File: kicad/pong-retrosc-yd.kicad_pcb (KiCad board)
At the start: 2 copper layers, 55 x 88 mm, 24 parts, among them J1 RCA video (na placa), J4 chave A/B (painel), J5 pot P1 (painel), J6 pot P2 (painel), J7 START (painel), J8 RCA audio L (na placa), J9 RCA audio R (na placa), U1 RP2040 roxo 1 botao, U2 PAM8403 HW-012

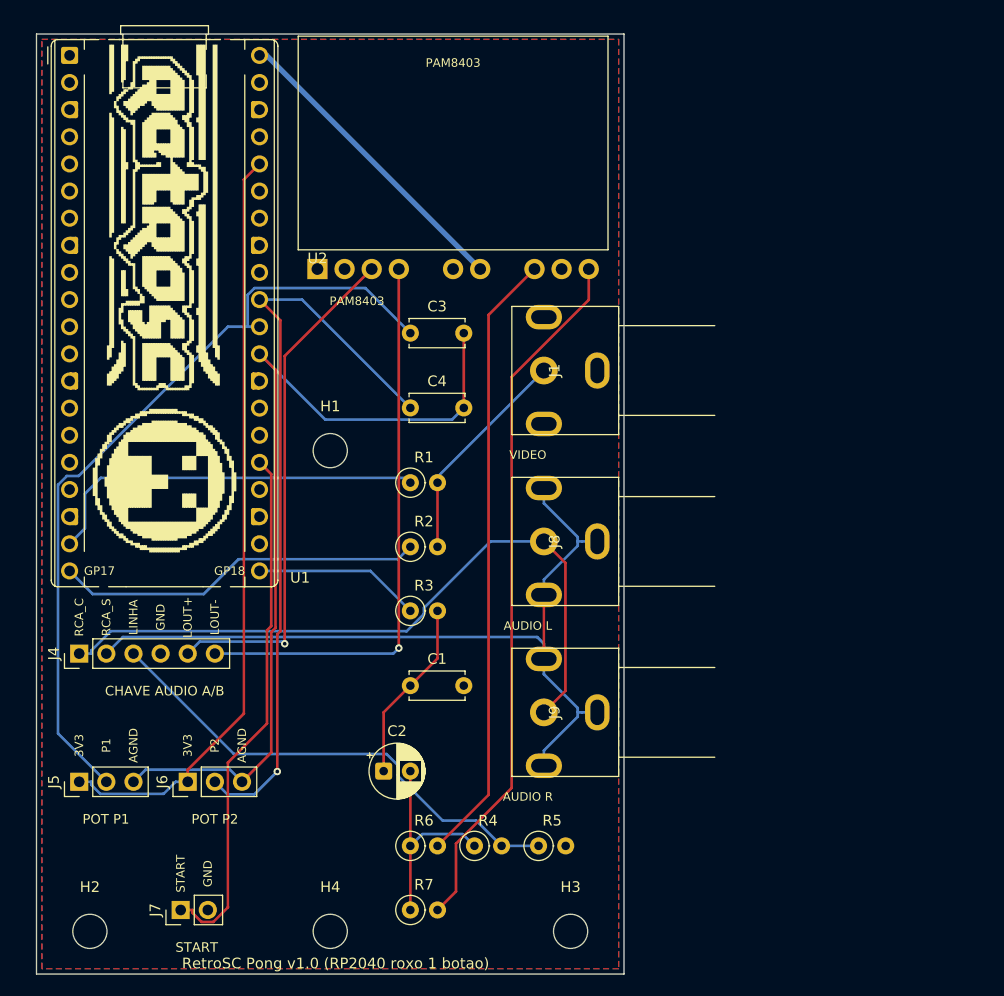
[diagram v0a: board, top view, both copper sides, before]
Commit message: kicad: placa 80x66 para a caixa Patola PB-085/3 (DRC 0 erros)
A placa era 55 x 88 e nao entrava na caixa. Agora e 80 x 66, contra os
~82 x 70 internos da PB-085/3 (85 x 73 x 32 montada).

Furacao refeita para os bossos da TAMPA: eram 4 furos M3 em losango de
45 mm; agora sao 2 furos a 58 mm entre centros, na linha de centro da
largura -- que e o que a caixa oferece (2 bossos com furo-guia o2,5, a
58 mm, no meio do lado de 85 mm). Em troca, o miolo das bordas de cima e
de baixo (x 36,5..43,5) virou area reservada.

Rearranjo, ja que a placa deitou (80 no maior lado):
- Pico a esquerda, USB na borda de cima; PAM8403 no topo a direita, com o
  pot saindo pela mesma borda
- os 3 RCAs desceram para a borda direita abaixo do amp
- os headers de painel foram para UMA fileira na borda de baixo (duas nao
  cabem: cada uma precisa de ~9 mm com os rotulos de funcao)
- rotulos dos headers centralizados sobre cada conector (PCB_TEXT e
  centrado na coordenada -- antes "CHAVE AUDIO A/B" saia cortado)

As duas variantes roteiam com 0 erros e 0 desconectados; gerbers, ZIPs e
imagens regenerados. Docs atualizados com as dimensoes, a furacao e o
aviso de que RCAs, pot e USB atravessam as paredes da caixa.

Co-Authored-By: Claude Opus 5 <noreply@anthropic.com>
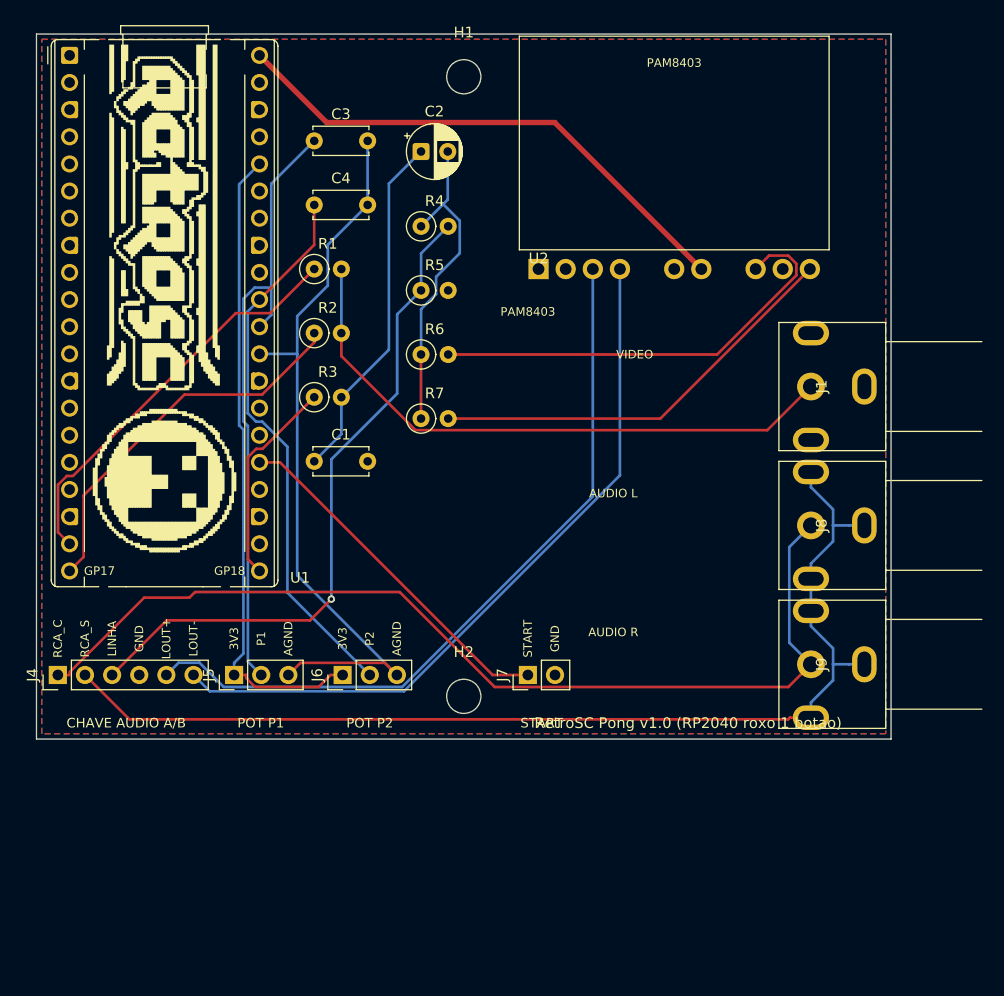
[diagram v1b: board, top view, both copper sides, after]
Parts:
- removed H3, H4: MountingHole_3.2mm_M3, MountingHole_3.2mm_M3
- moved R4 58.2 mm to (56.0, 38.0)
- moved C2 58.1 mm to (56.0, 31.0)
- moved R5 53.2 mm to (56.0, 44.0)
- moved R6 46.0 mm to (56.0, 50.0)
- moved R7 46.0 mm to (56.0, 56.0)
- moved H2 41.3 mm to (60.0, 82.0)
- moved J7 39.2 mm to (66.0, 80.0)
- moved H1 37.2 mm to (60.0, 24.0)
- moved J9 25.4 mm to (92.5, 79.0)
- moved J1 25.0 mm to (92.5, 53.0)
- moved J8 25.0 mm to (92.5, 66.0)
- moved C1 22.8 mm to (46.0, 60.0)
- moved R1 21.9 mm to (46.0, 42.0)
- moved R2 21.9 mm to (46.0, 48.0)
- moved R3 21.9 mm to (46.0, 54.0)
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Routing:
- net COMPOSITE: track 20.6 -> 56.7 mm
- net RCA_C: track 66.0 -> 93.1 mm
- net AMP_R: track 65.9 -> 39.7 mm
- net RCA_S: track 78.2 -> 102.0 mm
- net LOUT_P: track 48.1 -> 70.0 mm, vias 1 -> 0
- net +5V: track 28.9 -> 49.6 mm
- net POT2: track 70.6 -> 51.6 mm, vias 1 -> 0
- net LINHA: track 45.9 -> 62.9 mm, vias 0 -> 1
- net POT1: track 74.9 -> 58.5 mm
- net AMP_L: track 57.8 -> 41.4 mm
- net AUD_F: track 17.1 -> 33.1 mm
- net START: track 49.4 -> 33.4 mm
- net LOUT_N: track 52.9 -> 68.2 mm, vias 1 -> 0
- net +3V3: track 71.9 -> 60.4 mm
- net AGND: track 82.2 -> 71.2 mm
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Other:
- board size 55 x 88 mm -> 80 x 66 mm

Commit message: kicad: cobre longe dos parafusos e serigrafia corrigida
Dois problemas apontados na revisao da placa.

1. Trilhas rentes aos furos de montagem: o roteador passava sinal a 2,0 mm
   do centro do furo -- 0,4 mm da borda, debaixo da cabeca do parafuso.
   Agora cada furo tem uma AREA DE EXCLUSAO de raio 3,6 mm (rule area nas
   2 faces) barrando trilha e via; o plano de GND continua entrando, que
   encostar em GND e inofensivo. A trilha mais proxima passou de 2,0 para
   3,9 mm. make_decoy.py preserva as rule areas (antes removia todas as
   zonas, e o roteador nao as via).

2. Serigrafia:
   - GP17/GP18 nao diziam QUAL pino, ao lado de 20 pads iguais: agora tem
     linha de chamada ate o pad, comecando fora do contorno do modulo
   - VIDEO/AUDIO L/AUDIO R estavam soltos no meio da placa, a 17 mm dos
     jacks: foram para junto de cada um, com a referencia (ex.: "VIDEO (J1)")
   - referencias que caiam sobre pads (J1/J4..J9, H1/H2, U2) ocultadas ou
     movidas -- a informacao esta nos rotulos descritivos
   - contorno do footprint do RCA cruzava as proprias abas de terra: as
     laterais agora sao quebradas na altura dos pads
   - logo reescalado (0,22 -> 0,19 mm/px) para caber ENTRE as duas linhas
     verticais do footprint do Pico, que ele atravessava
   - texto de versao foi para a area livre do meio (o da variante YD nao
     cabia no rodape)

   silk_over_copper 11 -> 0, silk_overlap 30 -> 0. Sobram 12 avisos de
   borda: USB e barris dos RCAs cruzando o contorno, que e intencional.

Na variante YD o roteador agora recebe 0,17 mm de isolamento: pedindo os
0,15 do projeto ele entregava 0,1478 e o DRC reprovava.

DRC: 0 erros nas duas placas. Gerbers, ZIPs, renders e desenho de encaixe
regenerados.

Co-Authored-By: Claude Opus 5 <noreply@anthropic.com>
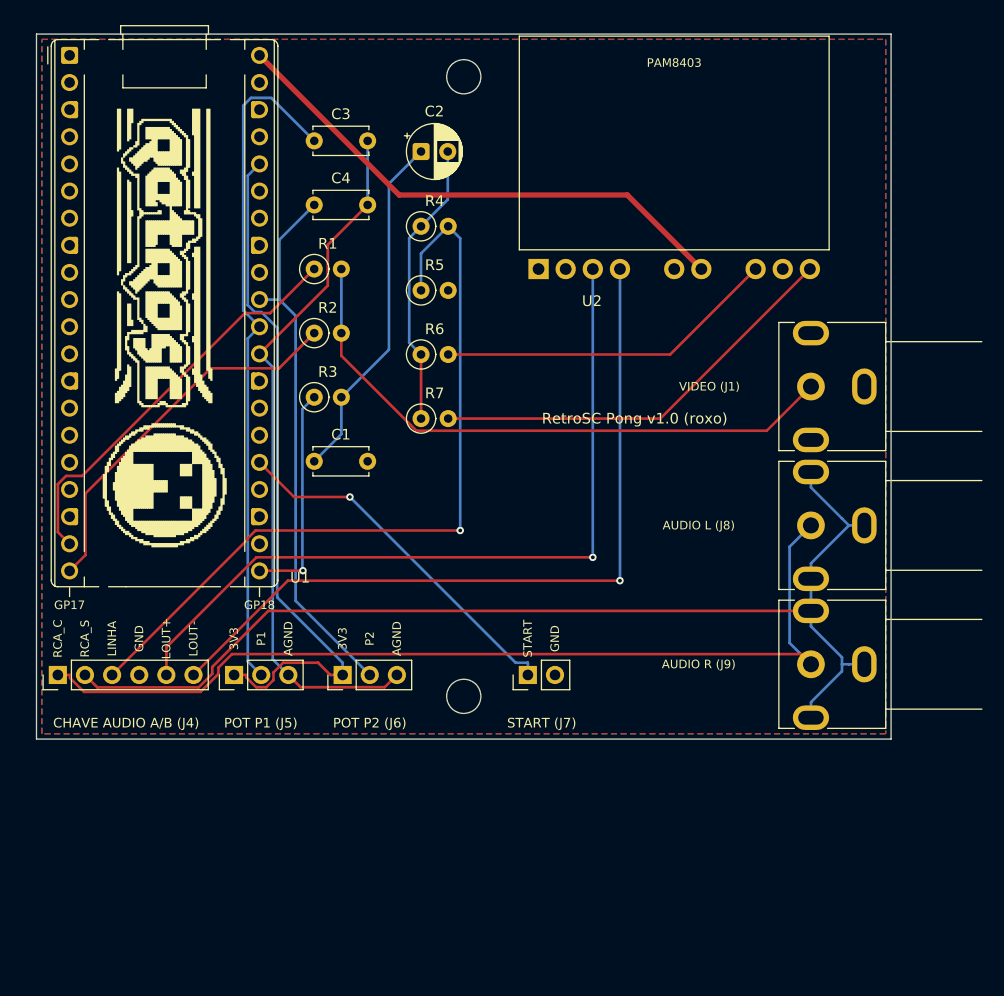
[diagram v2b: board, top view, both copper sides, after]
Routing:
- net LINHA: track 62.9 -> 74.2 mm
- net AMP_L: track 41.4 -> 32.1 mm
- net POT1: track 58.5 -> 63.5 mm
- net RCA_C: track 93.1 -> 88.2 mm
- net AGND: track 71.2 -> 66.4 mm
- net +3V3: track 60.4 -> 65.0 mm
- net LOUT_N: track 68.2 -> 72.7 mm, vias 0 -> 1
- net AUD_C: track 30.3 -> 27.0 mm
- net LOUT_P: track 70.0 -> 73.0 mm, vias 0 -> 1
- net RCA_S: track 102.0 -> 103.7 mm
- net AUDIO_PWM: track 19.6 -> 20.8 mm, vias 0 -> 1
- net POT2: track 51.6 -> 50.7 mm
- net START: track 33.4 -> 34.0 mm, vias 0 -> 1
- net VIDEO: track 36.0 -> 35.5 mm
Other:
- board text added: "AUDIO L (J8)"
- board text added: "AUDIO R (J9)"
- board text added: "CHAVE AUDIO A/B (J4)"
- board text added: "POT P1 (J5)"
- board text added: "POT P2 (J6)"
- board text added: "RetroSC Pong v1.0 (roxo)"
- board text added: "START (J7)"
- board text added: "VIDEO (J1)"
- board text removed: "AUDIO L"
- board text removed: "AUDIO R"
- board text removed: "CHAVE AUDIO A/B"
- board text removed: "PAM8403"
- board text removed: "POT P1"
- board text removed: "POT P2"
- board text removed: "RetroSC Pong v1.0 (RP2040 roxo 1 botao)"
- board text removed: "VIDEO"

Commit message: kicad: afasta os headers na borda de baixo
J4 e J5 ficavam a 0,26 mm um do outro e as descricoes ("CHAVE AUDIO A/B
(J4)" / "POT P1 (J5)") corriam juntas.

Nao dava para so espacar: J4+J5+J6 ocupavam 35,0 mm dos 36,4 disponiveis
ate a area de exclusao do furo, e o par J5/J6 e indivisivel (a vaga entre
eles existe para um unico conector femea 1x7 servir os dois). Entao quem
mudou de lugar foi o START, que e independente:

  antes:  J4  J5 J6 ......... J7
  agora:  J4 ..... J7 ..... J5 J6      (o par a direita do furo)

Folgas: 7,8 mm entre J4 e J7 e 14,9 mm entre J7 e J5. O rotulo do J9
subiu, que o par passou a ocupar a faixa onde ele estava.

DRC 0 erros nas duas placas; serigrafia sem sobreposicao nem silk sobre
cobre. Gerbers, ZIPs, renders e desenho de encaixe regenerados.

Co-Authored-By: Claude Opus 5 <noreply@anthropic.com>
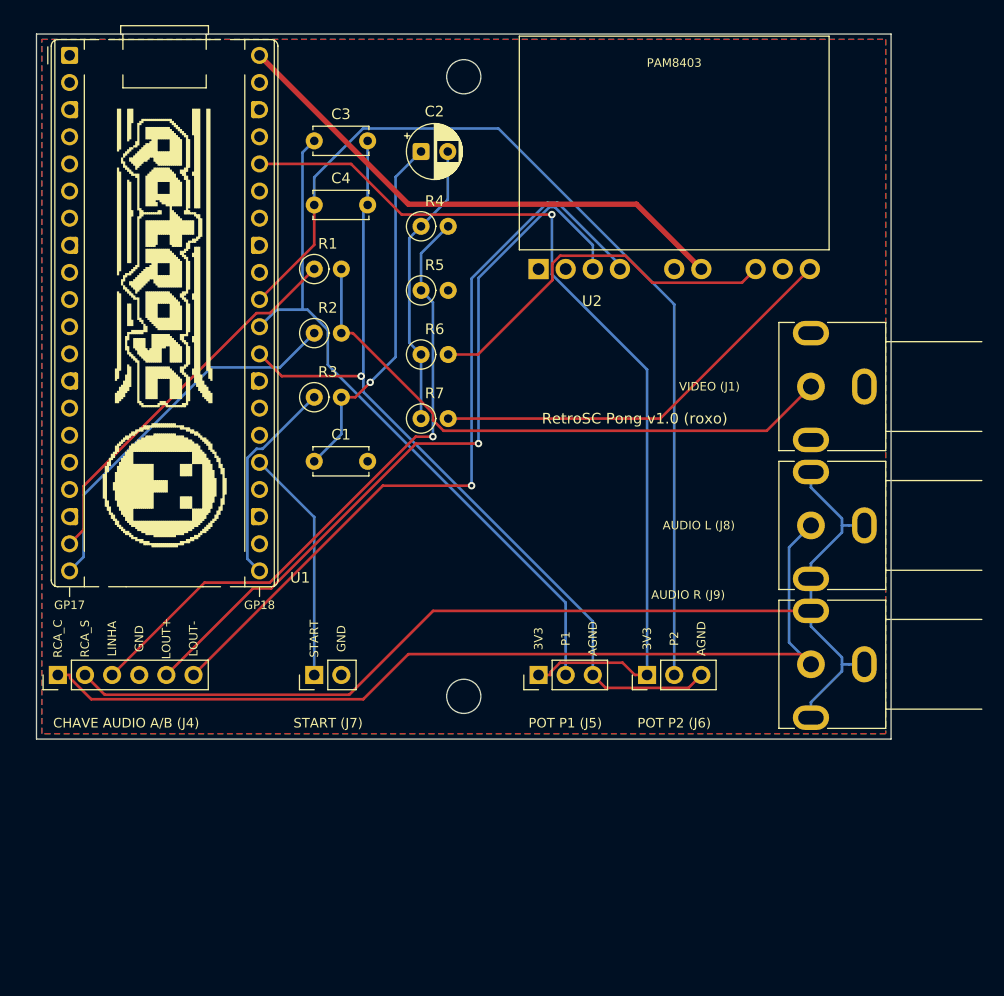
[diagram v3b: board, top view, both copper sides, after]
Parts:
- moved J5 28.5 mm to (67.0, 80.0)
- moved J6 28.5 mm to (77.2, 80.0)
- moved J7 20.0 mm to (46.0, 80.0)
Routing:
- net POT2: track 50.7 -> 90.7 mm
- net +3V3: track 65.0 -> 87.4 mm, vias 0 -> 1
- net AGND: track 66.4 -> 80.8 mm, vias 0 -> 1
- net LINHA: track 74.2 -> 60.5 mm
- net START: track 34.0 -> 22.0 mm, vias 1 -> 0
- net AMP_L: track 32.1 -> 35.1 mm
- net SYNC: track 38.4 -> 35.9 mm
- net LOUT_P: track 73.0 -> 70.9 mm
- net POT1: track 63.5 -> 65.6 mm
- net AUDIO_PWM: track 20.8 -> 19.7 mm, vias 1 -> 0
- net COMPOSITE: track 56.7 -> 55.8 mm
- net AUD_F: track 33.1 -> 33.9 mm, vias 0 -> 1

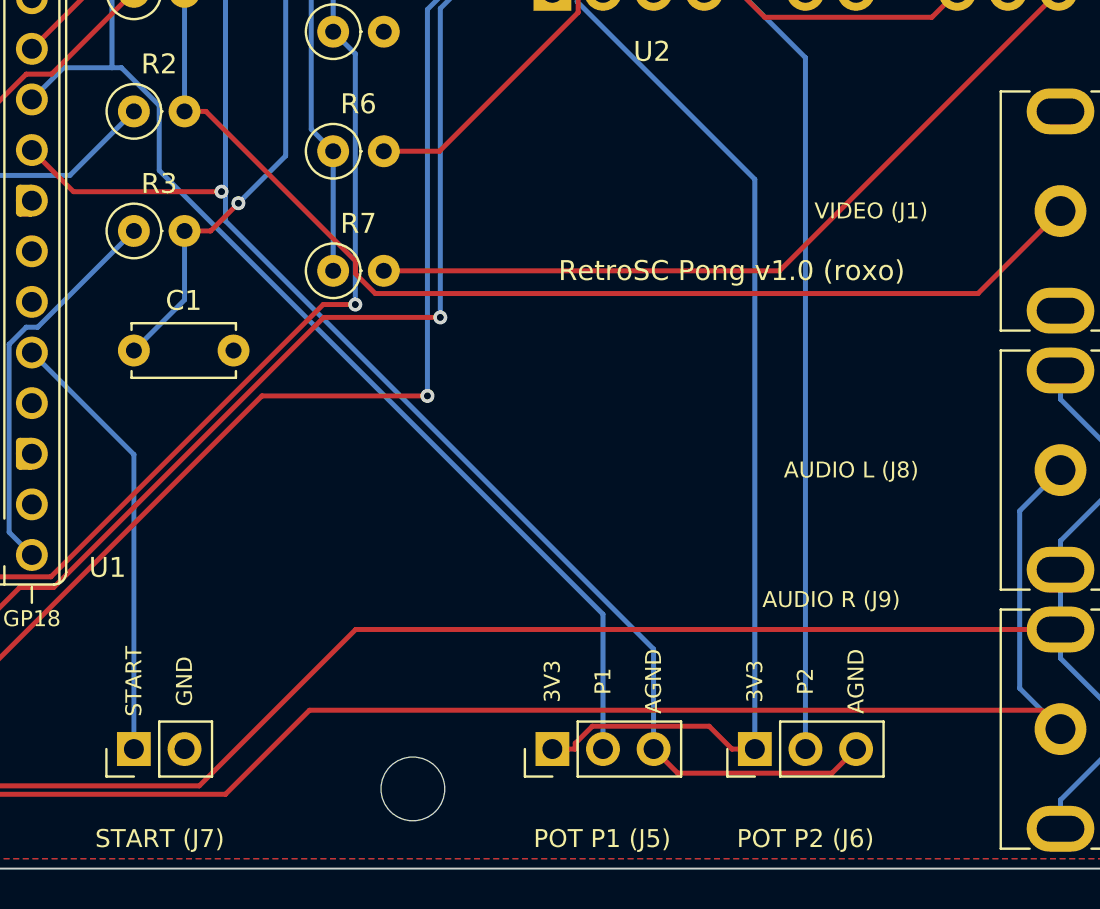
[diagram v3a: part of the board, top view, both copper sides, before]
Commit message: kicad: rotulos dos RCAs na vertical e assinatura no meio da placa
- VIDEO/AUDIO L/AUDIO R passam a ser verticais (rot 90), encostados na
  lateral de cada jack: acompanham a altura do conector, ficam sem duvida
  de qual e qual e nao disputam espaco com a faixa dos headers. O
  "AUDIO R" em especial estava solto, longe do seu jack.
- assinatura na area vazia do centro: "RetroSC Pong v1.0" em 1,6 mm e
  "LRRosa 2026" em 1,1 mm logo abaixo.

DRC 0 erros nas duas placas, sem silk sobre cobre nem sobreposicao.
Gerbers, ZIPs, renders e desenho de encaixe regenerados.

Co-Authored-By: Claude Opus 5 <noreply@anthropic.com>
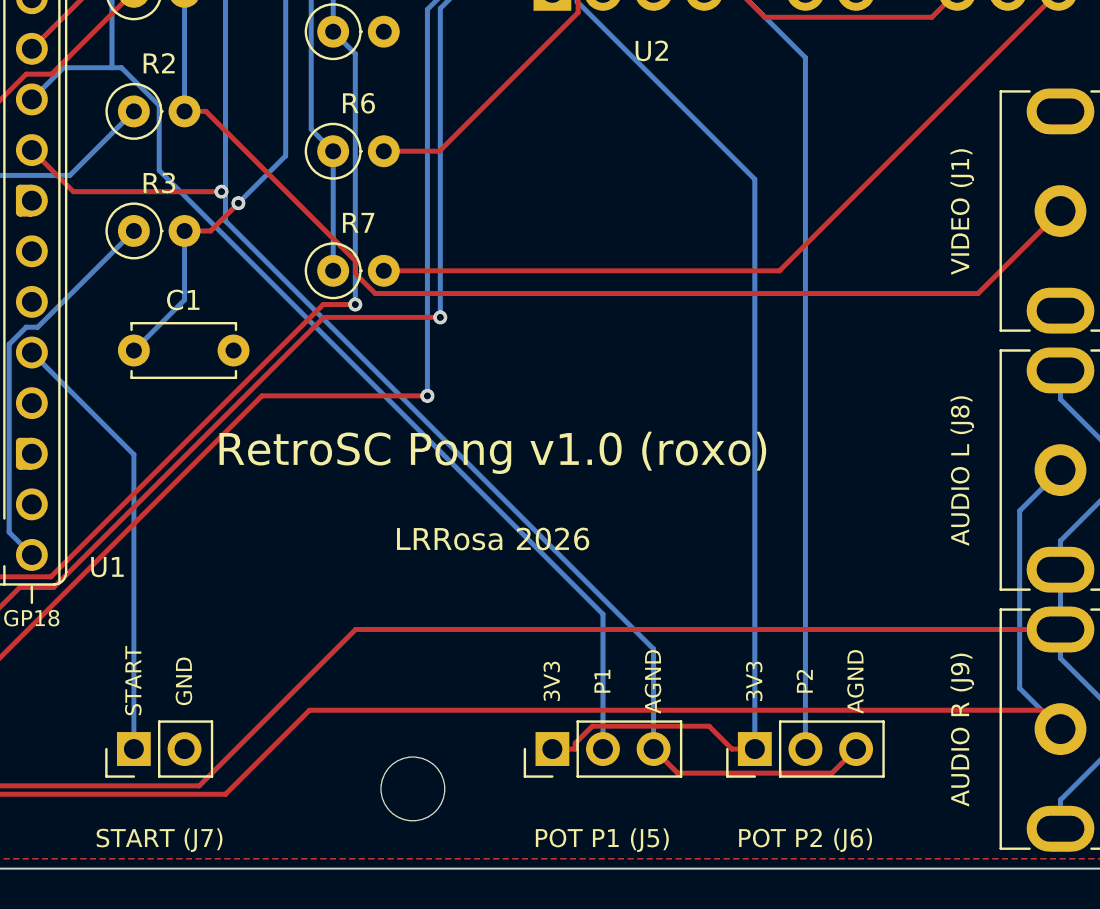
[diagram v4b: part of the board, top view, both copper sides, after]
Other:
- board text added: "LRRosa 2026"
